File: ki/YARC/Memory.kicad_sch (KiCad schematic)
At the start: 15 parts, among them U100 74LS32, U14 74LS20, U18 AS6C6264, U20 74HC00, U21 74LS08, U22 74LS139, U23 74LS32, U24 AS6C6264, U25 74HC245, U26 74LS157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

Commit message: Schematic for addressing unit is complete and all ERC violations addressed
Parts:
- removed U31: 74LS32, symbol 74xx:74LS32
- added unit 4 of U21
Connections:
- net GND: now also U21.12, U21.13
- net ~{MEM16} renamed ~{M16_EN}
- no-connect marks 4 -> 5
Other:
- note removed: "74LS08 "D" unit is also uncommitted. It was accidentally deleted here."
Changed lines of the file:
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@@
   (junction (at 228.6 170.18) (diameter 0) (color 0 0 0 0)
   )
-  (junction (at 27.94 144.78) (diameter 0) (color 0 0 0 0)
+  (junction (at 203.2 182.88) (diameter 0) (color 0 0 0 0)
   )
-  (junction (at 200.66 170.18) (diameter 0) (color 0 0 0 0)
+  (junction (at 27.94 144.78) (diameter 0) (color 0 0 0 0)
   )
   (junction (at 157.48 182.88) (diameter 0) (color 0 0 0 0)
@@
   (junction (at 256.54 144.78) (diameter 0) (color 0 0 0 0)
   )
-  (junction (at 186.69 144.78) (diameter 0) (color 0 0 0 0)
-  )
   (junction (at 214.63 170.18) (diameter 0) (color 0 0 0 0)
   )
   (junction (at 68.58 27.94) (diameter 0) (color 0 0 0 0)
   )
+  (junction (at 182.88 185.42) (diameter 0) (color 0 0 0 0)
+  )
+  (junction (at 200.66 170.18) (diameter 0) (color 0 0 0 0)
+  )
   (junction (at 110.49 185.42) (diameter 0) (color 0 0 0 0)
   )
@@
   )
   (no_connect (at 198.12 180.34))
+  (no_connect (at 218.44 180.34))
   (no_connect (at 73.66 86.36))
   (no_connect (at 177.8 180.34))
@@
     (stroke (width 0) (type default))
   )
-  (bus_entry (at 400.05 69.85) (size 2.54 2.54)
-    (stroke (width 0) (type default))
-  )
   (bus_entry (at 195.58 66.04) (size 2.54 2.54)
     (stroke (width 0) (type default))
@@
     (stroke (width 0) (type default))
   )
-  (wire (pts (xy 25.4 177.8) (xy 30.48 177.8))
+  (wire (pts (xy 26.67 177.8) (xy 30.48 177.8))
     (stroke (width 0) (type default))
   )
@@
     (stroke (width 0) (type default))
   )
-  (wire (pts (xy 149.86 185.42) (xy 149.86 182.88))
+  (wire (pts (xy 203.2 182.88) (xy 203.2 185.42))
     (stroke (width 0) (type default))
   )
-  (bus (pts (xy 213.36 15.24) (xy 215.9 15.24))
+  (wire (pts (xy 149.86 185.42) (xy 149.86 182.88))
     (stroke (width 0) (type default))
   )
-  (wire (pts (xy 157.48 170.18) (xy 200.66 170.18))
+  (bus (pts (xy 213.36 15.24) (xy 215.9 15.24))
     (stroke (width 0) (type default))
   )
@@
     (stroke (width 0) (type default))
   )
-  (wire (pts (xy 186.69 144.78) (xy 200.66 144.78))
+  (wire (pts (xy 182.88 144.78) (xy 200.66 144.78))
     (stroke (width 0) (type default))
   )
@@
     (stroke (width 0) (type default))
   )
+  (wire (pts (xy 182.88 185.42) (xy 203.2 185.42))
+    (stroke (width 0) (type default))
+  )
   (wire (pts (xy 162.56 182.88) (xy 157.48 182.88))
     (stroke (width 0) (type default))
@@
     (stroke (width 0) (type default))
   )
+  (wire (pts (xy 157.48 170.18) (xy 200.66 170.18))
+    (stroke (width 0) (type default))
+  )
   (bus (pts (xy 111.76 15.24) (xy 114.3 15.24))
     (stroke (width 0) (type default))
@@
     (stroke (width 0) (type default))
   )
-  (wire (pts (xy 182.88 144.78) (xy 186.69 144.78))
-    (stroke (width 0) (type default))
-  )
   (wire (pts (xy 157.48 17.78) (xy 157.48 30.48))
     (stroke (width 0) (type default))
@@
     (stroke (width 0) (type default))
   )
+  (wire (pts (xy 203.2 177.8) (xy 203.2 182.88))
+    (stroke (width 0) (type default))
+  )
   (bus (pts (xy 43.18 66.04) (xy 45.72 66.04))
     (stroke (width 0) (type default))
@@
     (effects (font (size 1.27 1.27)) (justify left bottom))
   )
-  (text "74LS08 \"D\" unit is also uncommitted.\nIt was accidentally deleted here."
-    (at 208.28 182.88 0)
-    (effects (font (size 1.27 1.27)) (justify left bottom))
-  )
   (text "Mem High <=> Sys Low" (at 177.8 96.52 0)
     (effects (font (size 1.27 1.27)) (justify left bottom))
@@
     )
   )
-  (global_label "~{MEM16}" (shape input) (at 25.4 177.8 180) (fields_autoplaced)
-    (effects (font (size 1.27 1.27)) (justify right))
-    (property "Intersheetrefs" "${INTERSHEET_REFS}" (at 16.5159 177.7206 0)
-      (effects (font (size 1.27 1.27)) (justify right) hide)
-    )
-  )
   (global_label "~{MEMWR_CLK}" (shape input) (at 30.48 50.8 270) (fields_autoplaced)
     (effects (font (size 1.27 1.27)) (justify right))
@@
     )
   )
+  (global_label "~{M16_EN}" (shape input) (at 26.67 177.8 180) (fields_autoplaced)
+    (effects (font (size 1.27 1.27)) (justify right))
+    (property "Intersheetrefs" "${INTERSHEET_REFS}" (at 16.3673 177.8 0)
+      (effects (font (size 1.27 1.27)) (justify right) hide)
+    )
+  )
   (global_label "~{CROSS_EN}" (shape input) (at 128.27 198.12 0) (fields_autoplaced)
     (effects (font (size 1.27 1.27)) (justify left))
@@
     )
   )
-  (symbol (lib_id "74xx:74LS32") (at 186.69 157.48 0) (unit 5)
-    (in_bom yes) (on_board yes) (dnp no)
-    (property "Reference" "U31" (at 187.96 147.32 0)
-      (effects (font (size 1.27 1.27)) (justify left))
-    )
-    (property "Value" "74LS32" (at 182.88 157.48 0)
-      (effects (font (size 1.27 1.27)) (justify left))
-    )
-    (property "Footprint" "" (at 186.69 157.48 0)
-      (effects (font (size 1.27 1.27)) hide)
-    )
-    (property "Datasheet" "http://www.ti.com/lit/gpn/sn74LS32" (at 186.69 157.48 0)
-      (effects (font (size 1.27 1.27)) hide)
-    )
-    (pin "1")
-    (pin "2")
-    (pin "3")
-    (pin "4")
-    (pin "5")
-    (pin "6")
-    (pin "10")
-    (pin "8")
-    (pin "9")
-    (pin "11")
-    (pin "12")
-    (pin "13")
-    (pin "14")
-    (pin "7")
-    (instances
-      (project "YARC"
-        (path "/22e0f8e1-b0d7-4d47-bb7c-8ef04cd95fca/32a6a89d-8e27-4c41-a8a1-866f443f001b"
-          (reference "U31") (unit 5)
-        )
-      )
-    )
-  )
   (symbol (lib_id "power:VCC") (at 246.38 40.64 0) (unit 1)
     (in_bom yes) (on_board yes) (dnp no) (fields_autoplaced)
@@
         )
       )
+    )
+  )
+  (symbol (lib_id "74xx:74LS08") (at 210.82 180.34 0) (unit 4)
+    (in_bom yes) (on_board yes) (dnp no)
+    (property "Reference" "U21" (at 210.82 175.26 0)
+      (effects (font (size 1.27 1.27)))
+    )
+    (property "Value" "74LS08" (at 210.82 180.34 0)
+      (effects (font (size 1.27 1.27)))
+    )
+    (property "Footprint" "" (at 210.82 180.34 0)
+      (effects (font (size 1.27 1.27)) hide)
+    )
+    (property "Datasheet" "http://www.ti.com/lit/gpn/sn74LS08" (at 210.82 180.34 0)
+      (effects (font (size 1.27 1.27)) hide)
+    )
+    (pin "1")
+    (pin "2")
+    (pin "3")
+    (pin "4")
+    (pin "5")
+    (pin "6")
+    (pin "10")
+    (pin "8")
+    (pin "9")
+    (pin "11")
+    (pin "12")
+    (pin "13")
+    (pin "14")
+    (pin "7")
+    (instances
+      (project "YARC"
+        (path "/22e0f8e1-b0d7-4d47-bb7c-8ef04cd95fca/32a6a89d-8e27-4c41-a8a1-866f443f001b"
+          (reference "U21") (unit 4)
+        )
+      )

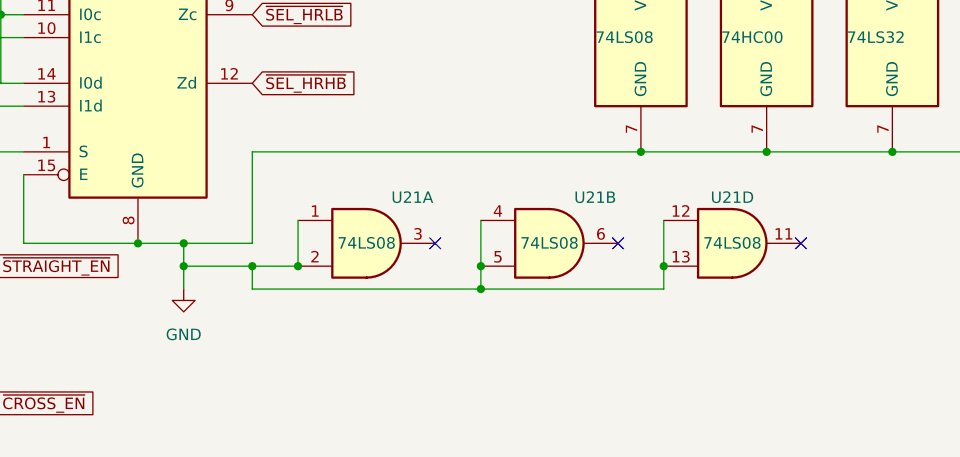
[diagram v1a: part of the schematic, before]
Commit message: Additional minor corrections. ERC clean.
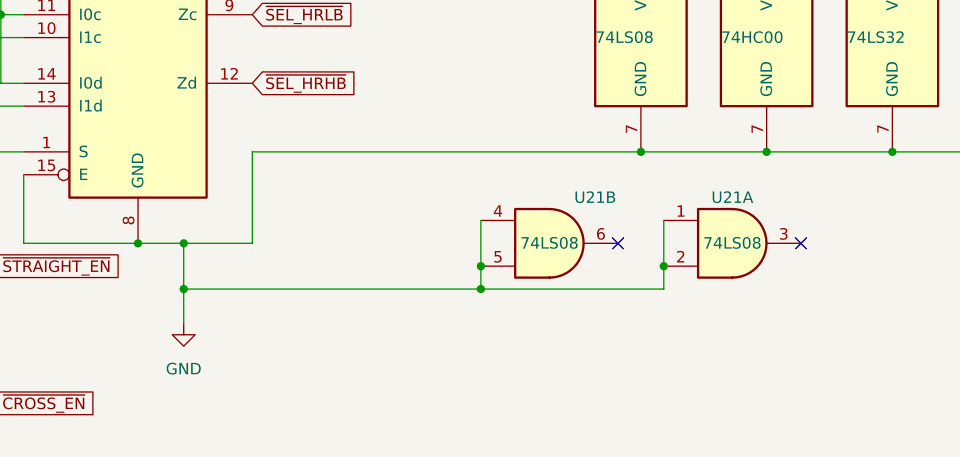
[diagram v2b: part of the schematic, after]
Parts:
- removed unit 1 of U21
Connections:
- net GND: now also U21.1, U21.2; no longer U21.12, U21.13
- no-connect marks 5 -> 4
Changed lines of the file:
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@@
   (junction (at 27.94 144.78) (diameter 0) (color 0 0 0 0)
   )
-  (junction (at 157.48 182.88) (diameter 0) (color 0 0 0 0)
-  )
   (junction (at 127 139.7) (diameter 0) (color 0 0 0 0)
   )
@@
   (junction (at 242.57 170.18) (diameter 0) (color 0 0 0 0)
   )
-  (junction (at 162.56 182.88) (diameter 0) (color 0 0 0 0)
-  )
   (junction (at 190.5 27.94) (diameter 0) (color 0 0 0 0)
   )
@@
   (junction (at 214.63 170.18) (diameter 0) (color 0 0 0 0)
   )
+  (junction (at 149.86 185.42) (diameter 0) (color 0 0 0 0)
+  )
   (junction (at 68.58 27.94) (diameter 0) (color 0 0 0 0)
   )
@@
   (junction (at 27.94 182.88) (diameter 0) (color 0 0 0 0)
   )
-  (junction (at 149.86 182.88) (diameter 0) (color 0 0 0 0)
-  )
   (junction (at 200.66 144.78) (diameter 0) (color 0 0 0 0)
   )
@@
   (no_connect (at 218.44 180.34))
   (no_connect (at 73.66 86.36))
-  (no_connect (at 177.8 180.34))
   (no_connect (at 73.66 88.9))
   (bus_entry (at 152.4 15.24) (size 2.54 2.54)
@@
     (stroke (width 0) (type default))
   )
-  (wire (pts (xy 149.86 185.42) (xy 149.86 182.88))
+  (wire (pts (xy 149.86 189.23) (xy 149.86 185.42))
     (stroke (width 0) (type default))
   )
@@
     (stroke (width 0) (type default))
   )
-  (wire (pts (xy 149.86 182.88) (xy 149.86 180.34))
+  (wire (pts (xy 149.86 180.34) (xy 149.86 185.42))
     (stroke (width 0) (type default))
   )
@@
     (stroke (width 0) (type default))
   )
-  (wire (pts (xy 162.56 182.88) (xy 157.48 182.88))
-    (stroke (width 0) (type default))
-  )
   (wire (pts (xy 142.24 27.94) (xy 142.24 40.64))
     (stroke (width 0) (type default))
@@
     (stroke (width 0) (type default))
   )
-  (wire (pts (xy 157.48 185.42) (xy 157.48 182.88))
-    (stroke (width 0) (type default))
-  )
-  (wire (pts (xy 182.88 185.42) (xy 157.48 185.42))
-    (stroke (width 0) (type default))
-  )
   (wire (pts (xy 50.8 180.34) (xy 66.04 180.34))
     (stroke (width 0) (type default))
@@
     (stroke (width 0) (type default))
   )
-  (wire (pts (xy 162.56 177.8) (xy 162.56 182.88))
-    (stroke (width 0) (type default))
-  )
   (wire (pts (xy 203.2 177.8) (xy 203.2 182.88))
     (stroke (width 0) (type default))
@@
     (stroke (width 0) (type default))
   )
-  (wire (pts (xy 157.48 182.88) (xy 149.86 182.88))
+  (wire (pts (xy 149.86 185.42) (xy 182.88 185.42))
     (stroke (width 0) (type default))
   )
@@
     )
   )
-  (symbol (lib_id "74xx:74LS08") (at 170.18 180.34 0) (unit 1)
-    (in_bom yes) (on_board yes) (dnp no)
-    (property "Reference" "U21" (at 175.26 175.26 0)
-      (effects (font (size 1.27 1.27)))
-    )
-    (property "Value" "74LS08" (at 170.18 180.34 0)
-      (effects (font (size 1.27 1.27)))
-    )
-    (property "Footprint" "" (at 170.18 180.34 0)
-      (effects (font (size 1.27 1.27)) hide)
-    )
-    (property "Datasheet" "http://www.ti.com/lit/gpn/sn74LS08" (at 170.18 180.34 0)
-      (effects (font (size 1.27 1.27)) hide)
-    )
-    (pin "1")
-    (pin "2")
-    (pin "3")
-    (pin "4")
-    (pin "5")
-    (pin "6")
-    (pin "10")
-    (pin "8")
-    (pin "9")
-    (pin "11")
-    (pin "12")
-    (pin "13")
-    (pin "14")
-    (pin "7")
-    (instances
-      (project "YARC"
-        (path "/22e0f8e1-b0d7-4d47-bb7c-8ef04cd95fca/32a6a89d-8e27-4c41-a8a1-866f443f001b"
-          (reference "U21") (unit 1)
-        )
-      )
-    )
-  )
   (symbol (lib_id "pdxjjb:AS6C6264") (at 101.6 40.64 270) (unit 1)
     (in_bom yes) (on_board yes) (dnp no)
@@
     )
   )
-  (symbol (lib_id "power:GND") (at 149.86 185.42 0) (unit 1)
+  (symbol (lib_id "power:GND") (at 149.86 189.23 0) (unit 1)
     (in_bom yes) (on_board yes) (dnp no) (fields_autoplaced)
-    (property "Reference" "#PWR0107" (at 149.86 191.77 0)
+    (property "Reference" "#PWR0107" (at 149.86 195.58 0)
       (effects (font (size 1.27 1.27)) hide)
     )
-    (property "Value" "GND" (at 149.86 190.5 0)
+    (property "Value" "GND" (at 149.86 194.31 0)
       (effects (font (size 1.27 1.27)))
     )
-    (property "Footprint" "" (at 149.86 185.42 0)
+    (property "Footprint" "" (at 149.86 189.23 0)
       (effects (font (size 1.27 1.27)) hide)
     )
-    (property "Datasheet" "" (at 149.86 185.42 0)
+    (property "Datasheet" "" (at 149.86 189.23 0)
       (effects (font (size 1.27 1.27)) hide)
     )
@@
     )
   )
-  (symbol (lib_id "74xx:74LS08") (at 210.82 180.34 0) (unit 4)
+  (symbol (lib_id "74xx:74LS08") (at 210.82 180.34 0) (unit 1)
     (in_bom yes) (on_board yes) (dnp no)
     (property "Reference" "U21" (at 210.82 175.26 0)
@@
       (project "YARC"
         (path "/22e0f8e1-b0d7-4d47-bb7c-8ef04cd95fca/32a6a89d-8e27-4c41-a8a1-866f443f001b"
-          (reference "U21") (unit 4)
+          (reference "U21") (unit 1)
         )
       )
